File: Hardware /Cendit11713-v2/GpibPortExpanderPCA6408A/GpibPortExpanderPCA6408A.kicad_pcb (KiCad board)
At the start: 2 copper layers, 26 parts, among them P1 CONN_01X07, U1 PCA6408A, U2 PCA6408A

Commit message: Cendit11713 respaldo del trabajo en PCBs
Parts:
- added C5: 0.1uF, Capacitors_SMD:C_0805_HandSoldering, F.Cu at (132.0, 113.6)
- added C6: 0.1uF, Capacitors_SMD:C_0805_HandSoldering, F.Cu at (132.1, 116.1)
- added C7: 0.1uF, Capacitors_SMD:C_0805_HandSoldering, F.Cu at (136.7, 92.3)
- added C8: 0.1uF, Capacitors_SMD:C_0805_HandSoldering, F.Cu at (134.5, 92.2)
- moved C3 50.4 mm to (125.2, 85.3), turned to 180 degrees
- moved C4 50.1 mm to (126.0, 82.4)
- moved C1 39.4 mm to (125.2, 91.7), turned to 180 degrees
- moved C2 38.4 mm to (125.9, 88.4), turned to 180 degrees
- moved R1 10.3 mm to (132.5, 109.4), turned to 180 degrees
- moved CONN2 4.83 mm to (160.7, 89.9)
- moved R10 4.83 mm to (168.4, 89.8)
- moved R11 4.83 mm to (168.4, 92.3)
- moved R12 4.83 mm to (168.4, 94.9)
- moved R13 4.83 mm to (168.4, 97.4)
- moved R14 4.83 mm to (168.4, 99.9)
- moved R15 4.83 mm to (168.4, 102.5)
- moved R16 4.83 mm to (168.4, 105.0)
- moved R17 4.83 mm to (168.4, 107.6)
- moved R2 4.83 mm to (155.7, 89.8)
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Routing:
- net GNDD: track 2.38 -> 300.6 mm, vias 1 -> 6
- net +5V: track 0.00 -> 105.3 mm, vias 0 -> 5
- net +3V3: track 0.00 -> 82.4 mm, vias 0 -> 5
- net //RESET: track 0.00 -> 72.8 mm, vias 0 -> 2
- net /SCL: track 0.00 -> 65.3 mm, vias 0 -> 2
- net /SDA: track 0.00 -> 58.4 mm, vias 0 -> 2
- net /PIFC: track 0.00 -> 54.2 mm, vias 0 -> 2
- net /PREN: track 0.00 -> 49.3 mm, vias 0 -> 2
- net //INT: track 0.00 -> 47.4 mm, vias 0 -> 3
- net /PATN: track 0.00 -> 46.1 mm
- net /PSRQ: track 0.00 -> 42.7 mm, vias 0 -> 2
- net /PDAV: track 0.00 -> 41.0 mm
- net /PNDAC: track 0.00 -> 35.7 mm
- net /PEOI: track 0.00 -> 34.7 mm, vias 0 -> 2
- net /PNRFD: track 0.00 -> 30.5 mm
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- added copper zone on F.Cu, net GNDD

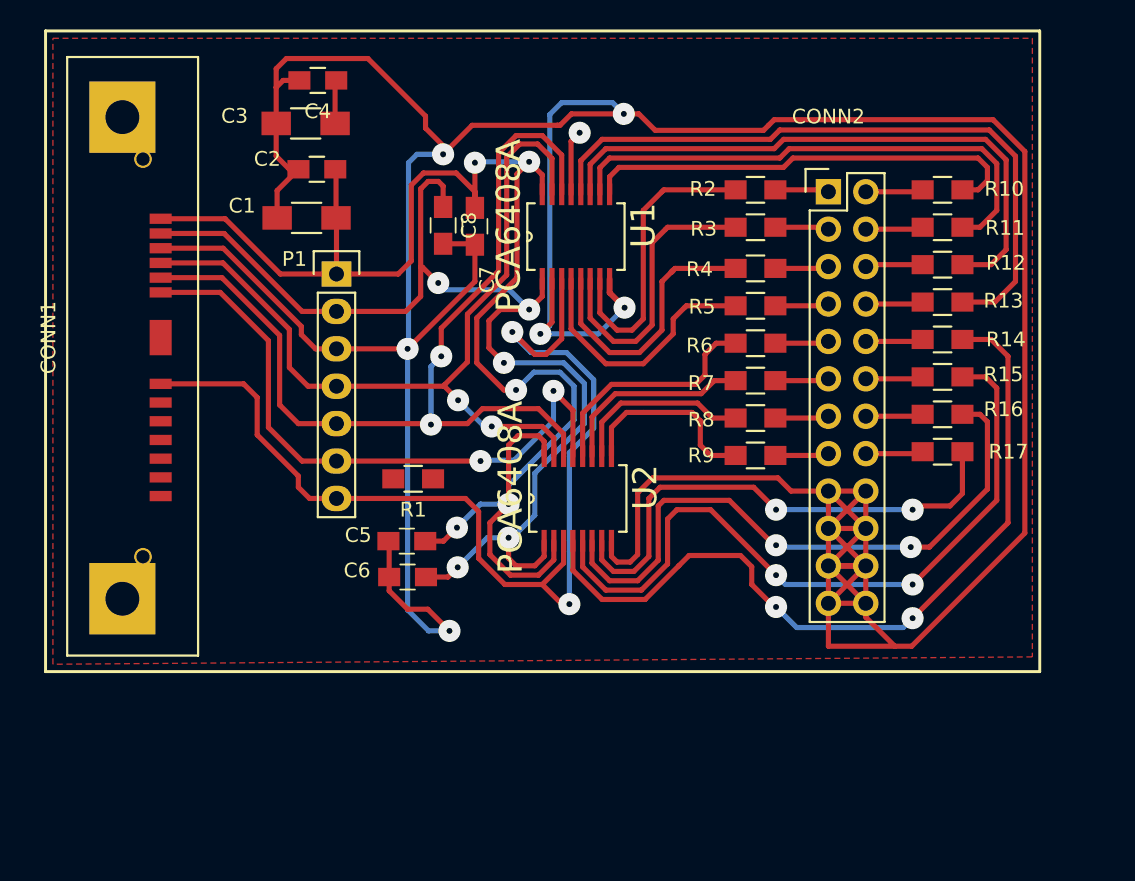
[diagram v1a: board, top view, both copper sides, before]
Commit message: En Cendit11713 edicion de esquematicos + revision PCBs
  - Edicion de esquematicos tarjeta madre
  - Revision de PCBs corrección de footprints
  - Descarga de footprints + creacion lib simbolos: RTC + sensor temp/hum
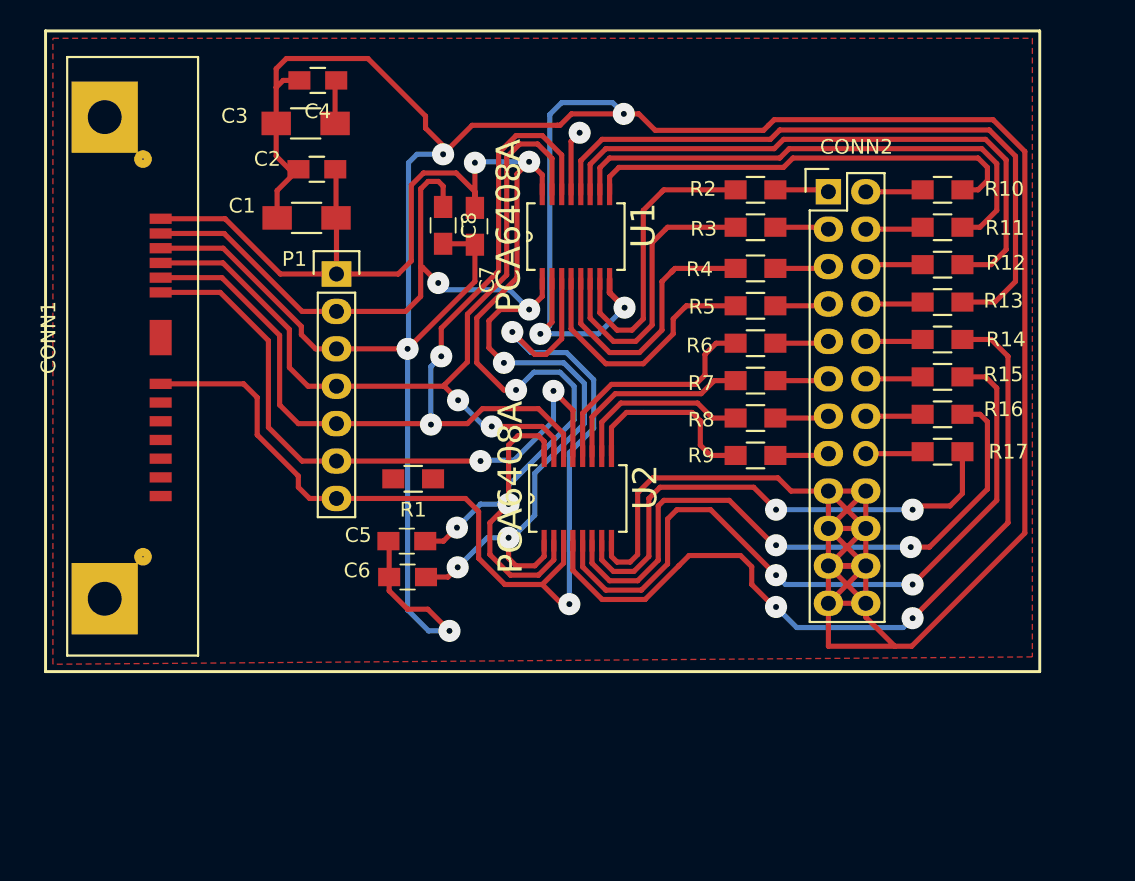
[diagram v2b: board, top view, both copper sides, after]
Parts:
- CONN2: footprint Pin_Headers:Pin_Header_Straight_2x12 -> CenditFootprints:GPIB_HEADER_12X2P
